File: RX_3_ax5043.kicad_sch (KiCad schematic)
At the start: 16 parts, among them U405 AX5043, U406 TPS22929D

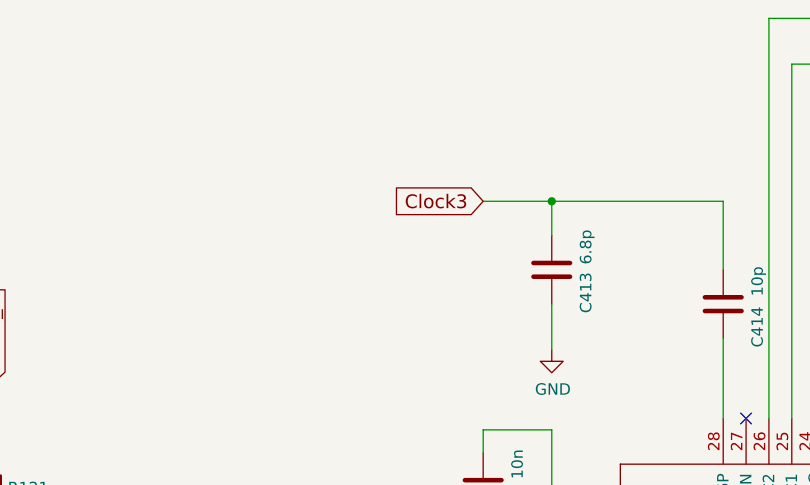
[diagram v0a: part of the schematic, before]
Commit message: Wire in clocks, more cleanups, wire in MRAM
Signed-off-by: Corey Minyard <corey@minyard.net>
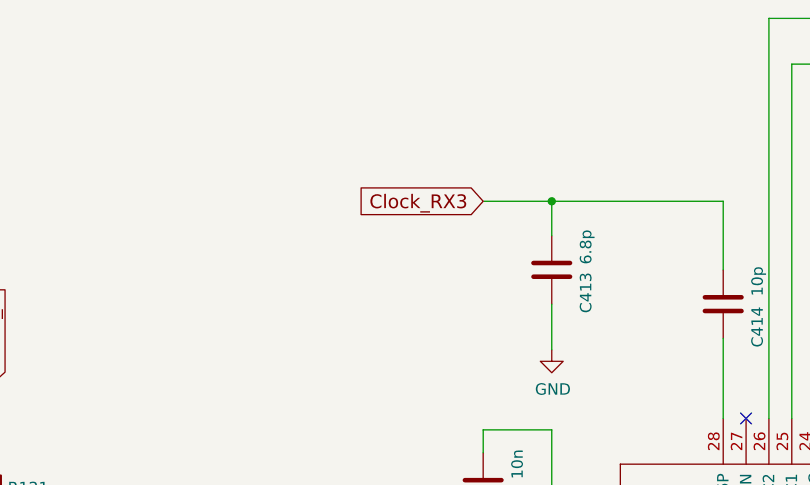
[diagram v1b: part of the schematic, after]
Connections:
- net Clock3 renamed Clock_RX3
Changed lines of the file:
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@@
 		)
 	)
-	(global_label "Clock3"
+	(global_label "Clock_RX3"
 		(shape input)
 		(at 234.95 76.2 180)
@@
 		)
 		(property "Intersheetrefs" "${INTERSHEET_REFS}"
-			(at 224.556 76.2 0)
+			(at 220.3241 76.2 0)
 			(effects
 				(font

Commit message: Finish up and clean up a lot of things
Signed-off-by: Corey Minyard <corey@minyard.net>
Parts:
- added R129: 1K, Resistor_SMD:R_0603_1608Metric_Pad0.98x0.95mm_HandSolder, symbol Device:R
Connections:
- net AX5043_CLK: now also R129.2; no longer U405.15 (CLK)
- new net: R129.1, U405.15 (CLK)
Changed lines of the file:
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@@
 	(wire
 		(pts
-			(xy 293.37 132.08) (xy 297.18 132.08)
+			(xy 308.61 132.08) (xy 317.5 132.08)
+		)
+		(stroke
+			(width 0)
+			(type default)
+		)
+	)
+	(wire
+		(pts
+			(xy 293.37 132.08) (xy 300.99 132.08)
 		)
 		(stroke
@@
 	(global_label "AX5043_CLK"
 		(shape input)
-		(at 297.18 132.08 0)
+		(at 317.5 132.08 0)
 		(fields_autoplaced yes)
 		(effects
@@
 		)
 		(property "Intersheetrefs" "${INTERSHEET_REFS}"
-			(at 313.8875 132.08 0)
+			(at 334.2075 132.08 0)
 			(effects
 				(font
@@
 					(unit 1)
 				)
+			)
+		)
+	)
+	(symbol
+		(lib_id "Device:R")
+		(at 304.8 132.08 90)
+		(unit 1)
+		(exclude_from_sim no)
+		(in_bom yes)
+		(on_board yes)
+		(dnp no)
+		(property "Reference" "R129"
+			(at 305.054 134.366 90)
+			(effects
+				(font
+					(size 1.27 1.27)
+				)
+			)
+		)
+		(property "Value" "1K"
+			(at 305.054 136.906 90)
+			(effects
+				(font
+					(size 1.27 1.27)
+				)
+			)
+		)
+		(property "Footprint" "Resistor_SMD:R_0603_1608Metric_Pad0.98x0.95mm_HandSolder"
+			(at 304.8 133.858 90)
+			(effects
+				(font
+					(size 1.27 1.27)
+				)
+				(hide yes)
+			)
+		)
+		(property "Datasheet" "~"
+			(at 304.8 132.08 0)
+			(effects
+				(font
+					(size 1.27 1.27)
+				)
+				(hide yes)
+			)
+		)
+		(property "Description" "Resistor"
+			(at 304.8 132.08 0)
+			(effects
+				(font
+					(size 1.27 1.27)
+				)
+				(hide yes)
+			)
+		)
+		(pin "1"
+		)
+		(pin "2"
+		)
+		(instances
+			(project "PacSat_AFSK"
+				(path "/cc9f42d2-6985-41ac-acab-5ab7b01c5b38/9432d45f-be08-406b-8d9c-bfe62f690c2f"
+					(reference "R129")
+					(unit 1)
+				)

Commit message: Add a CPU thermsistor
Signed-off-by: Corey Minyard <corey@minyard.net>
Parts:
- C450: footprint Capacitor_SMD:C_0402_1005Metric -> Capacitor_SMD:C_0603_1608Metric_Pad1.08x0.95mm_HandSolder
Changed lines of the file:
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@@
 			)
 		)
-		(property "Footprint" "Capacitor_SMD:C_0402_1005Metric"
+		(property "Footprint" "Capacitor_SMD:C_0603_1608Metric_Pad1.08x0.95mm_HandSolder"
 			(at 350.2152 77.47 0)
 			(effects

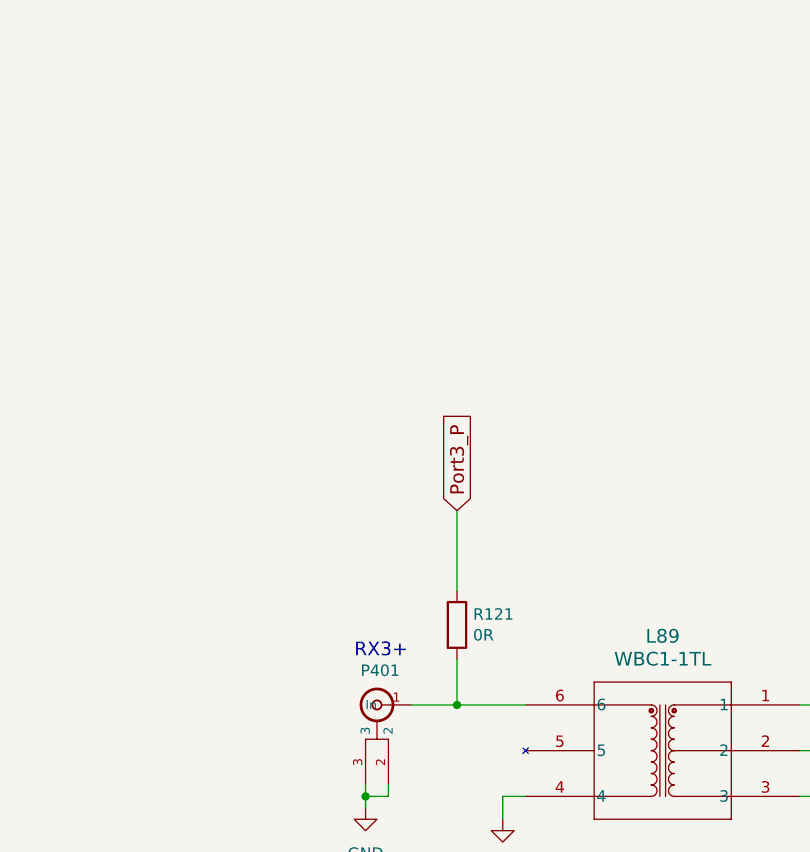
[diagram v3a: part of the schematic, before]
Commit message: Add shields around AX5043s, replace UFL connectors
Signed-off-by: Corey Minyard <corey@minyard.net>
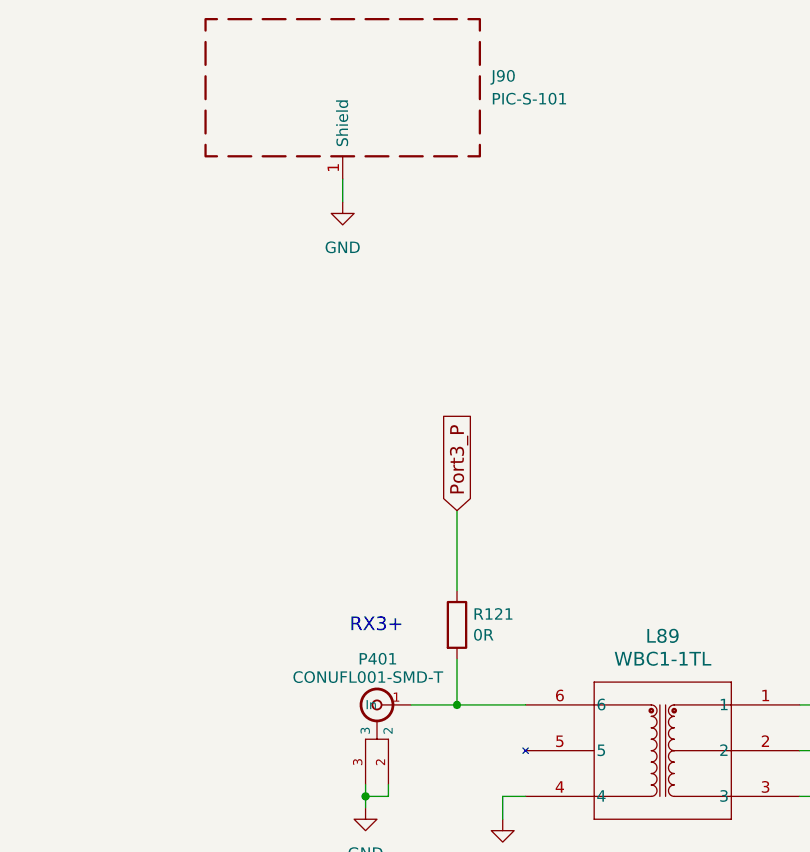
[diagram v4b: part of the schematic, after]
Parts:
- added J90: PIC-S-101, PacSatDev_misc:RF_SHIELD_PIC_S_101, symbol Device:RFShield_OnePiece
- P401: value ~ -> CONUFL001-SMD-T; footprint PacSatDev_misc:U_FL -> PacSatDev_misc:CONN1_CONUFL_TEC
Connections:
- net GND: now also J90.1 (Shield)
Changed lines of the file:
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@@
 	(text "RX3+"
 		(exclude_from_sim no)
-		(at 168.91 113.03 0)
+		(at 168.402 110.236 0)
 		(effects
 			(font
@@
 		(pts
 			(xy 234.95 76.2) (xy 242.57 76.2)
+		)
+		(stroke
+			(width 0)
+			(type default)
+		)
+	)
+	(wire
+		(pts
+			(xy 167.64 59.69) (xy 167.64 62.23)
 		)
 		(stroke
@@
 	)
 	(symbol
+		(lib_id "Device:RFShield_OnePiece")
+		(at 167.64 49.53 0)
+		(unit 1)
+		(exclude_from_sim no)
+		(in_bom yes)
+		(on_board yes)
+		(dnp no)
+		(fields_autoplaced yes)
+		(property "Reference" "J90"
+			(at 184.15 48.2599 0)
+			(effects
+				(font
+					(size 1.27 1.27)
+				)
+				(justify left)
+			)
+		)
+		(property "Value" "PIC-S-101"
+			(at 184.15 50.7999 0)
+			(effects
+				(font
+					(size 1.27 1.27)
+				)
+				(justify left)
+			)
+		)
+		(property "Footprint" "PacSatDev_misc:RF_SHIELD_PIC_S_101"
+			(at 167.64 52.07 0)
+			(effects
+				(font
+					(size 1.27 1.27)
+				)
+				(hide yes)
+			)
+		)
+		(property "Datasheet" "~"
+			(at 167.64 52.07 0)
+			(effects
+				(font
+					(size 1.27 1.27)
+				)
+				(hide yes)
+			)
+		)
+		(property "Description" "One-piece EMI RF shielding cabinet"
+			(at 167.64 49.53 0)
+			(effects
+				(font
+					(size 1.27 1.27)
+				)
+				(hide yes)
+			)
+		)
+		(pin "1"
+		)
+		(instances
+			(project "PacSat_AFSK"
+				(path "/cc9f42d2-6985-41ac-acab-5ab7b01c5b38/9432d45f-be08-406b-8d9c-bfe62f690c2f"
+					(reference "J90")
+					(unit 1)
+				)
+			)
+		)
+	)
+	(symbol
 		(lib_id "power:GND")
 		(at 242.57 92.71 0)
@@
 	)
 	(symbol
+		(lib_id "power:GND")
+		(at 167.64 62.23 0)
+		(unit 1)
+		(exclude_from_sim no)
+		(in_bom yes)
+		(on_board yes)
+		(dnp no)
+		(fields_autoplaced yes)
+		(property "Reference" "#PWR0198"
+			(at 167.64 68.58 0)
+			(effects
+				(font
+					(size 1.27 1.27)
+				)
+				(hide yes)
+			)
+		)
+		(property "Value" "GND"
+			(at 167.64 67.31 0)
+			(effects
+				(font
+					(size 1.27 1.27)
+				)
+			)
+		)
+		(property "Footprint" ""
+			(at 167.64 62.23 0)
+			(effects
+				(font
+					(size 1.27 1.27)
+				)
+				(hide yes)
+			)
+		)
+		(property "Datasheet" ""
+			(at 167.64 62.23 0)
+			(effects
+				(font
+					(size 1.27 1.27)
+				)
+				(hide yes)
+			)
+		)
+		(property "Description" ""
+			(at 167.64 62.23 0)
+			(effects
+				(font
+					(size 1.27 1.27)
+				)
+			)
+		)
+		(pin "1"
+		)
+		(instances
+			(project "PacSat_AFSK"
+				(path "/cc9f42d2-6985-41ac-acab-5ab7b01c5b38/9432d45f-be08-406b-8d9c-bfe62f690c2f"
+					(reference "#PWR0198")
+					(unit 1)
+				)
+			)
+		)
+	)
+	(symbol
 		(lib_id "Device:C")
 		(at 238.76 142.24 0)
@@
 		(dnp no)
 		(property "Reference" "P401"
-			(at 173.99 114.3 0)
+			(at 173.736 113.03 0)
 			(effects
 				(font
@@
 			)
 		)
-		(property "Value" "~"
+		(property "Value" "CONUFL001-SMD-T"
+			(at 170.434 115.062 0)
+			(effects
+				(font
+					(size 1.27 1.27)
+				)
+			)
+		)
+		(property "Footprint" "PacSatDev_misc:CONN1_CONUFL_TEC"
 			(at 171.45 118.11 0)
 			(effects
-				(font
-					(size 1.27 1.27)
-				)
-			)
-		)
-		(property "Footprint" "PacSatDev_misc:U_FL"
-			(at 171.45 118.11 0)
-			(effects

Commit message: More messing with RF shields
Signed-off-by: Corey Minyard <corey@minyard.net>
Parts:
- J90: value PIC-S-101 -> PIC-S-201F
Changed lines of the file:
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@@
 			)
 		)
-		(property "Value" "PIC-S-101"
+		(property "Value" "PIC-S-201F"
 			(at 184.15 50.7999 0)
 			(effects

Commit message: Update SPI clock with simulation
Simulated the SPI clocks, updated resistor values based on findings.

Signed-off-by: Corey Minyard <corey@minyard.net>
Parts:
- R129: value 1K -> 470
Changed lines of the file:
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@@
 			)
 		)
-		(property "Value" "1K"
+		(property "Value" "470"
 			(at 305.054 136.906 90)
 			(effects

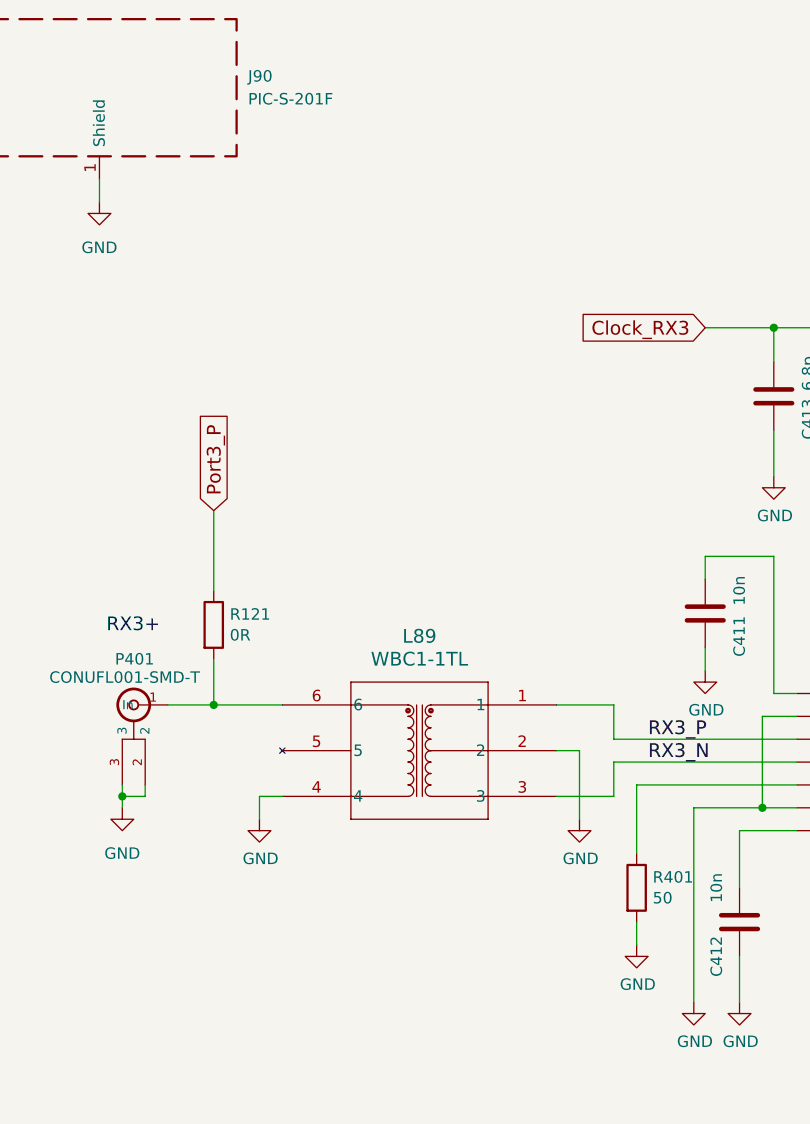
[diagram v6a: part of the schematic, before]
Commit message: Rework the AX5043 RX side to a different balun
It's cheaper (though not smaller) and fits inside the shield.

Signed-off-by: Corey Minyard <corey@minyard.net>
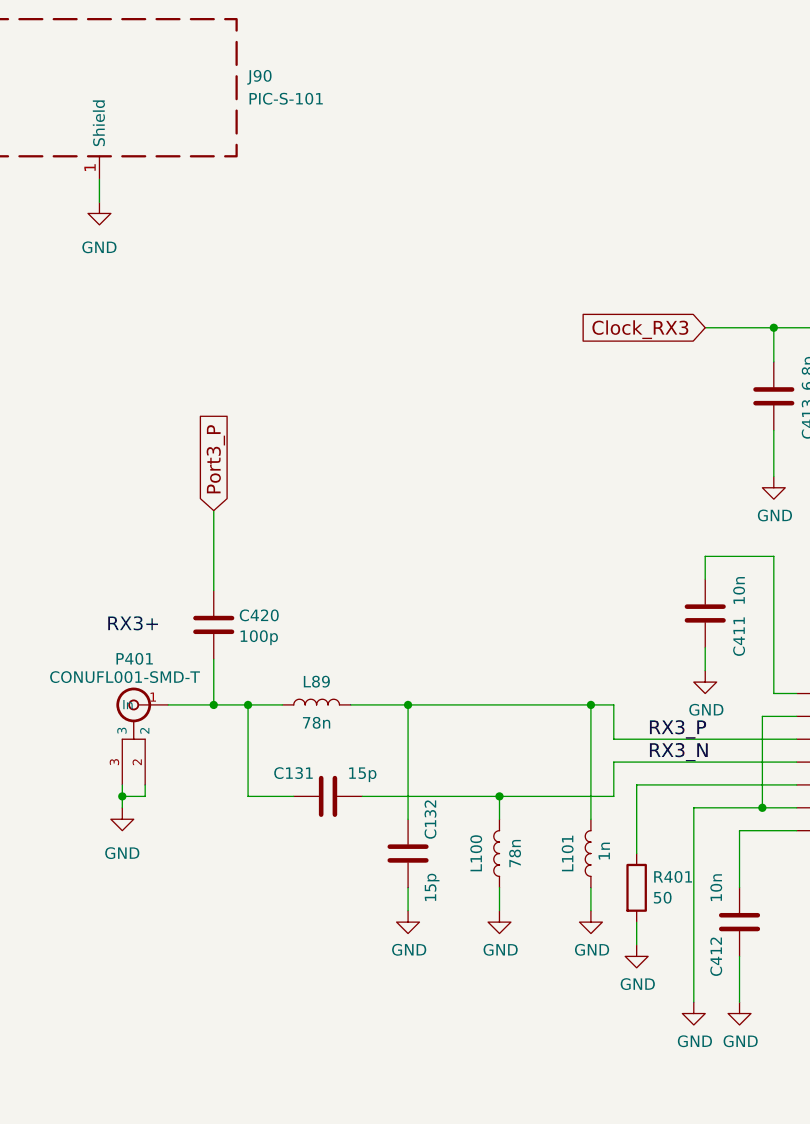
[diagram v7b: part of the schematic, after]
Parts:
- removed L89: WBC1-1TL, PacSatDev_misc:IND6_WBC1, symbol PACSAT_DEV_misc:WBC1-1TL
- added C131, C132: 15p, Capacitor_SMD:C_0603_1608Metric_Pad1.08x0.95mm_HandSolder, symbol Device:C
- added L100, L89: 78n, Inductor_SMD:L_0603_1608Metric_Pad1.05x0.95mm_HandSolder, symbol Device:L
- added L101: 1n, Inductor_SMD:L_0603_1608Metric_Pad1.05x0.95mm_HandSolder, symbol Device:L
- C420: renamed from R121; value 0R -> 100p; symbol Device:R -> Device:C
- J90: value PIC-S-201F -> PIC-S-101
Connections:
- net GND: now also C132.1, L100.1, L101.1
- net RX3_N: now also C131.1, L100.2
- net RX3_P: now also C132.2, L101.2, L89.2
- net at C420.2, P401.1 (In): now also C131.2, L89.1

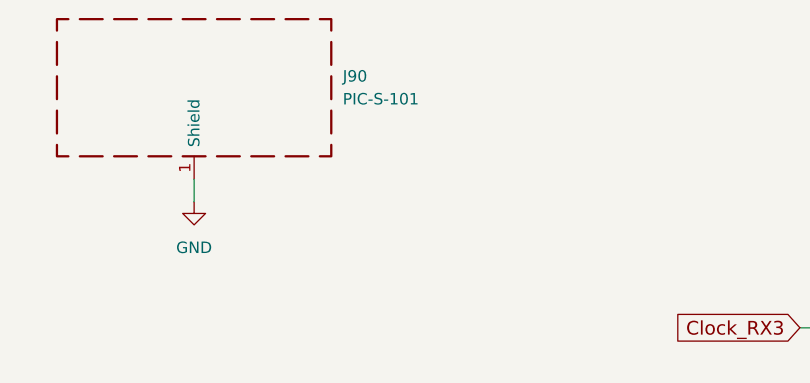
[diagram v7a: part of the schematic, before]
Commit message: Change the AX5043 shield to a frame/cover setup
Easier access to parts underneath.

Signed-off-by: Corey Minyard <corey@minyard.net>
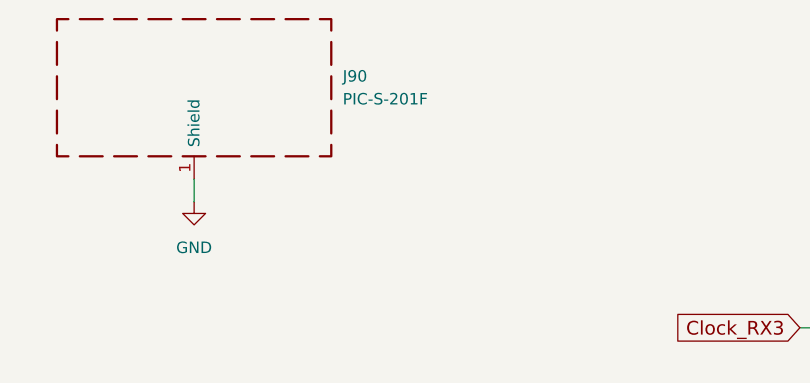
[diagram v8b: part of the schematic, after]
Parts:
- J90: value PIC-S-101 -> PIC-S-201F
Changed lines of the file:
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@@
 			)
 		)
-		(property "Value" "PIC-S-101"
+		(property "Value" "PIC-S-201F"
 			(at 184.15 50.7999 0)
 			(effects
